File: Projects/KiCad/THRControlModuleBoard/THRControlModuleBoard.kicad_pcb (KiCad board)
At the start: 2 copper layers, 137.4 x 137.4 mm, 63 parts, among them IC1 LTC1480CN8#PBF, IC2 LTC1480CN8#PBF, J1 Conn_01x02_Socket, J2 Conn_01x02_Socket, J3 PCC-SMP-K-5, J4 Screw_Terminal_01x02, J5 Conn_01x04_Socket, J6 Conn_01x04_Socket, Q1 Q_PMOS_GDS, Q2 Q_PMOS_GDS, Q3 Q_PMOS_GDS, U1 LTC4416EMS#PBF, U2 MAX31856MUD+T, U3 Value: MCP2562-E-P, U4 MCP2515-I/P, U5 MAX31855, Y1 8MHz

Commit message: 外形を大方決めた
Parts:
- removed the C1 at (85.2, 101.2)
- removed the C7 at (102.0, 113.5)
- removed the D1 at (75.4, 118.3)
- removed D5: LED, LED_SMD:LED_0805_2012Metric_Pad1.15x1.40mm_HandSolder
- removed the J1 at (79.9, 96.7)
- removed the J2 at (82.7, 120.3)
- removed JP3, JP4, JP5, JP6: SolderJumper_2_Bridged, Jumper:SolderJumper-2_P1.3mm_Open_TrianglePad1.0x1.5mm
- removed Q1, Q2, Q3: Q_PMOS_GDS, Package_TO_SOT_SMD:ATPAK-2
- removed the R1 at (75.4, 122.2)
- removed the R2 at (73.3, 107.5)
- removed the R5 at (79.9, 107.5)
- removed the R6 at (76.6, 107.5)
- removed the U1 at (85.2, 112.4)
- added C13: 0.1u, Capacitor_SMD:C_0805_2012Metric_Pad1.18x1.45mm_HandSolder, F.Cu at (243.9, 32.5)
- added C14: 0.1u, Capacitor_SMD:C_0805_2012Metric_Pad1.18x1.45mm_HandSolder, F.Cu at (243.9, 35.5)
- added C15: 0.1u, Capacitor_SMD:C_0805_2012Metric_Pad1.18x1.45mm_HandSolder, F.Cu at (243.9, 38.5)
- added C16: 0.1u, Capacitor_SMD:C_0805_2012Metric_Pad1.18x1.45mm_HandSolder, F.Cu at (243.9, 41.5)
- added C17: 0.1u, Capacitor_SMD:C_0805_2012Metric_Pad1.18x1.45mm_HandSolder, F.Cu at (243.9, 44.5)
- added C18: 0.1u, Capacitor_SMD:C_0805_2012Metric_Pad1.18x1.45mm_HandSolder, F.Cu at (243.9, 47.5)
- added D4: D, Diode_SMD:D_SOD-123, F.Cu at (242.4, 58.5)
- added J3: Conn_02x03_Odd_Even, Connector_PinHeader_2.00mm:PinHeader_2x03_P2.00mm_Vertical, F.Cu at (89.0, 135.8)
- added J4: Conn_02x03_Odd_Even, Connector_PinHeader_2.00mm:PinHeader_2x03_P2.00mm_Vertical, F.Cu at (256.4, 33.0)
- added J7: Conn_02x03_Odd_Even, Connector_PinHeader_2.00mm:PinHeader_2x03_P2.00mm_Vertical, F.Cu at (104.3, 113.4)
- added LS1: PKB24SPCH3601-B0, PKB24SPCH3601-B0:SPKR_PKB24SPCH3601-B0, F.Cu at (193.8, 129.3)
- added R11: 10k, Resistor_SMD:R_0603_1608Metric_Pad0.98x0.95mm_HandSolder, F.Cu at (217.8, 60.6)
- added R12: 1k, Resistor_SMD:R_0603_1608Metric_Pad0.98x0.95mm_HandSolder, F.Cu at (217.8, 63.1)
- added R13: 10k, Resistor_SMD:R_0603_1608Metric_Pad0.98x0.95mm_HandSolder, F.Cu at (217.8, 65.6)
- added R14: 10k, Resistor_SMD:R_0603_1608Metric_Pad0.98x0.95mm_HandSolder, F.Cu at (217.8, 68.1)
- added R15: 10k, Resistor_SMD:R_0603_1608Metric_Pad0.98x0.95mm_HandSolder, F.Cu at (217.8, 70.6)
- added R16: 10k, Resistor_SMD:R_0603_1608Metric_Pad0.98x0.95mm_HandSolder, F.Cu at (222.2, 58.1)
- added R17: 10k, Resistor_SMD:R_0603_1608Metric_Pad0.98x0.95mm_HandSolder, F.Cu at (222.2, 60.6)
- added R18: 10k, Resistor_SMD:R_0603_1608Metric_Pad0.98x0.95mm_HandSolder, F.Cu at (222.2, 63.1)
- added R19: 10k, Resistor_SMD:R_0603_1608Metric_Pad0.98x0.95mm_HandSolder, F.Cu at (222.2, 65.6)
- added R20: 10k, Resistor_SMD:R_0603_1608Metric_Pad0.98x0.95mm_HandSolder, F.Cu at (222.2, 68.1)
- added R21: 10k, Resistor_SMD:R_0603_1608Metric_Pad0.98x0.95mm_HandSolder, F.Cu at (222.2, 70.6)
- added R22: 1k, Resistor_SMD:R_0603_1608Metric_Pad0.98x0.95mm_HandSolder, F.Cu at (226.5, 58.1)
- added R23: 1k, Resistor_SMD:R_0603_1608Metric_Pad0.98x0.95mm_HandSolder, F.Cu at (226.5, 60.6)
- added R24: 1k, Resistor_SMD:R_0603_1608Metric_Pad0.98x0.95mm_HandSolder, F.Cu at (226.5, 63.1)
- added R25: 1k, Resistor_SMD:R_0603_1608Metric_Pad0.98x0.95mm_HandSolder, F.Cu at (226.5, 65.6)
- added R26: 1k, Resistor_SMD:R_0603_1608Metric_Pad0.98x0.95mm_HandSolder, F.Cu at (226.5, 68.1)
- added U4: TLP222A, Package_DIP:DIP-4_W7.62mm, F.Cu at (167.7, 117.9)
- C1: renamed from C2; footprint Capacitor_SMD:C_0805_2012Metric_Pad1.18x1.45mm_HandSolder -> Capacitor_SMD:C_0603_1608Metric_Pad1.08x0.95mm_HandSolder
- C10: renamed from C11; moved to B.Cu
- C11: renamed from C12; moved to B.Cu
- C12: renamed from C10; value 0.1μF -> 0.1μ; moved to B.Cu
- C2: renamed from C3; footprint Capacitor_SMD:C_0805_2012Metric_Pad1.18x1.45mm_HandSolder -> Capacitor_SMD:C_0603_1608Metric_Pad1.08x0.95mm_HandSolder
- C3: renamed from C4; footprint Capacitor_SMD:C_0805_2012Metric_Pad1.18x1.45mm_HandSolder -> Capacitor_SMD:C_0603_1608Metric_Pad1.08x0.95mm_HandSolder
- C4: renamed from C5; footprint Capacitor_SMD:C_0805_2012Metric_Pad1.18x1.45mm_HandSolder -> Capacitor_SMD:C_0603_1608Metric_Pad1.08x0.95mm_HandSolder
- C5: renamed from C6; footprint Capacitor_SMD:C_0805_2012Metric_Pad1.18x1.45mm_HandSolder -> Capacitor_SMD:C_0603_1608Metric_Pad1.08x0.95mm_HandSolder
- C6: renamed from C15; value 0.1μF -> 0.1u; footprint Capacitor_SMD:C_0805_2012Metric_Pad1.18x1.45mm_HandSolder -> Capacitor_SMD:C_0603_1608Metric_Pad1.08x0.95mm_HandSolder; moved to B.Cu
- C7: renamed from C8; value 0.1μF -> 0.1u; footprint Capacitor_SMD:C_0805_2012Metric_Pad1.18x1.45mm_HandSolder -> Capacitor_SMD:C_0603_1608Metric_Pad1.08x0.95mm_HandSolder
- C8: renamed from C9; value 0.1μF -> 0.1u; footprint Capacitor_SMD:C_0805_2012Metric_Pad1.18x1.45mm_HandSolder -> Capacitor_SMD:C_0603_1608Metric_Pad1.08x0.95mm_HandSolder
- C9: renamed from C14; value 0.1μF -> 0.1u; footprint Capacitor_SMD:C_0805_2012Metric_Pad1.18x1.45mm_HandSolder -> Capacitor_SMD:C_0603_1608Metric_Pad1.08x0.95mm_HandSolder; moved to B.Cu
- D1: renamed from D2; footprint Diode_SMD:D_0805_2012Metric_Pad1.15x1.40mm_HandSolder -> Diode_SMD:D_SOD-123
- D2: renamed from D3; footprint Diode_SMD:D_0805_2012Metric_Pad1.15x1.40mm_HandSolder -> Diode_SMD:D_SOD-123
- D3: renamed from D4; footprint Diode_SMD:D_0805_2012Metric_Pad1.15x1.40mm_HandSolder -> Diode_SMD:D_SOD-123
- J2: renamed from J4; footprint TerminalBlock:TerminalBlock_Altech_AK300-2_P5.00mm -> MAX31856MUD_T:RS_PRO_611-8157
- R10: value 1K -> 300; footprint LED_SMD:LED_0805_2012Metric_Pad1.15x1.40mm_HandSolder -> Resistor_SMD:R_0603_1608Metric_Pad0.98x0.95mm_HandSolder
- R6: renamed from R11; value 120Ω -> 120
- R7: renamed from R12; value 120Ω -> 120
- R8: renamed from R13; value 120Ω -> 120
- R9: renamed from R14; value 10kΩ -> 10k; moved to B.Cu
- U1: renamed from U2; footprint Package_SO:TSSOP-14_4.4x5mm_P0.65mm -> MAX31856MUD_T:SOP65P640X110-14N
- moved R10 149.5 mm to (217.8, 58.1)
- moved H4 121.4 mm to (226.9, 119.1)
- moved U5 103.3 mm to (78.2, 57.6), turned to 90 degrees
- moved JP1 83.9 mm to (234.3, 84.0), turned to 0 degrees
- moved H2 81.9 mm to (226.9, 98.0)
- moved JP2 79.3 mm to (234.3, 87.5), turned to 0 degrees
- moved H3 77.0 mm to (226.9, 108.5)
- moved J2 63.4 mm to (98.8, 34.4)
- moved G*** 55.1 mm to (88.3, 150.9)
- moved G*** 48.5 mm to (156.6, 178.4)
- moved C7 40.6 mm to (88.4, 96.7)
- moved IC1 40.6 mm to (89.7, 103.0)
- moved J6 40.6 mm to (77.2, 116.1)
- moved C8 40.6 mm to (88.3, 109.0)
- moved J5 40.6 mm to (77.2, 102.5)
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- renumbered J3 to J1, R3 to R1, R4 to R2, R7 to R3, R8 to R4, R9 to R5, U3 to U2, U4 to U3
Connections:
- net CAN_H renamed CAN__H
- net CAN_L renamed CAN__L
- A1 pad 10: unconnected-(A1-D7-Pad10) -> Umbilical__launchPin
- A1 pad 11: unconnected-(A1-D8-Pad11) -> Umbilical__waitingPin
- A1 pad 19: unconnected-(A1-A0-Pad19) -> B3M_Servo__Open
- A1 pad 20: unconnected-(A1-A1-Pad20) -> B3M_Servo__Close
- A1 pad 21: unconnected-(A1-A2-Pad21) -> RS405_Servo__Open
- A1 pad 22: unconnected-(A1-A3-Pad22) -> RS405_Servo__Close
- A1 pad 25: unconnected-(A1-A6-Pad25) -> IO__Busser
- A1 pad 30: +12V -> Net-(A1-VIN)
- A1 pad 6: MAX31855__~{CS}-~{CS} -> RS485__ENABLE_RS405
- A1 pad 8: RS485__ENABLE_RS405 -> MAX31855__~{CS}-~{CS}
- D1 pad 1: Net-(D2-K) -> SPI__MOSI
- D2 pad 1: Net-(D3-K) -> SPI__SCLK
- D3 pad 1: Net-(D4-K) -> MAX31856__~{CS}-~{CS}
- R10 pad 1: Net-(D5-A) -> IO__Busser
- U1 pad 11: Net-(JP6-A) -> SPI__MISO
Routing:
- net +3.3V: track 180.5 -> 74.6 mm, vias 5 -> 3
- net SPI__MISO: track 93.6 -> 8.61 mm, vias 4 -> 2
- net MAX31855__~{CS}-~{CS}: track 66.3 -> 0.00 mm, vias 1 -> 0
- net RS485__RO-RX: track 47.9 -> 0.00 mm, vias 1 -> 0
- net +12V: track 38.7 -> 0.00 mm
- net RS485__ENABLE_RS405: track 37.0 -> 0.00 mm, vias 3 -> 0
- net RS485__ENABLE_B3M: track 31.6 -> 0.00 mm
- net +5V: track 39.7 -> 10.1 mm, vias 1 -> 0
- net SPI__MOSI: track 32.4 -> 4.51 mm, vias 2 -> 0
- net External Power Supply: track 27.3 -> 0.00 mm, vias 2 -> 0
- net Net-(U1-E1): track 25.2 -> 0.00 mm
- net MAX31856__~{CS}-~{CS}: track 29.1 -> 4.11 mm, vias 2 -> 0
- net RS485__DI-TX: track 22.9 -> 0.22 mm
- net Net-(Q1-G): track 20.1 -> 0.00 mm, vias 2 -> 0
- net CAN__TXD-TXCAN: track 18.3 -> 0.00 mm
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- removed copper zone on F.Cu, net /QMOS/3-3
- removed copper zone on F.Cu, net External Power Supply
- removed copper zone on F.Cu, net Internal Power Supply
- removed copper zone on F.Cu, net Main Power Supply
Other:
- board size 137.4 x 137.4 mm -> 87.2 x 130 mm
- board text added: "~{CS}"
- board text removed: "Nano Every"

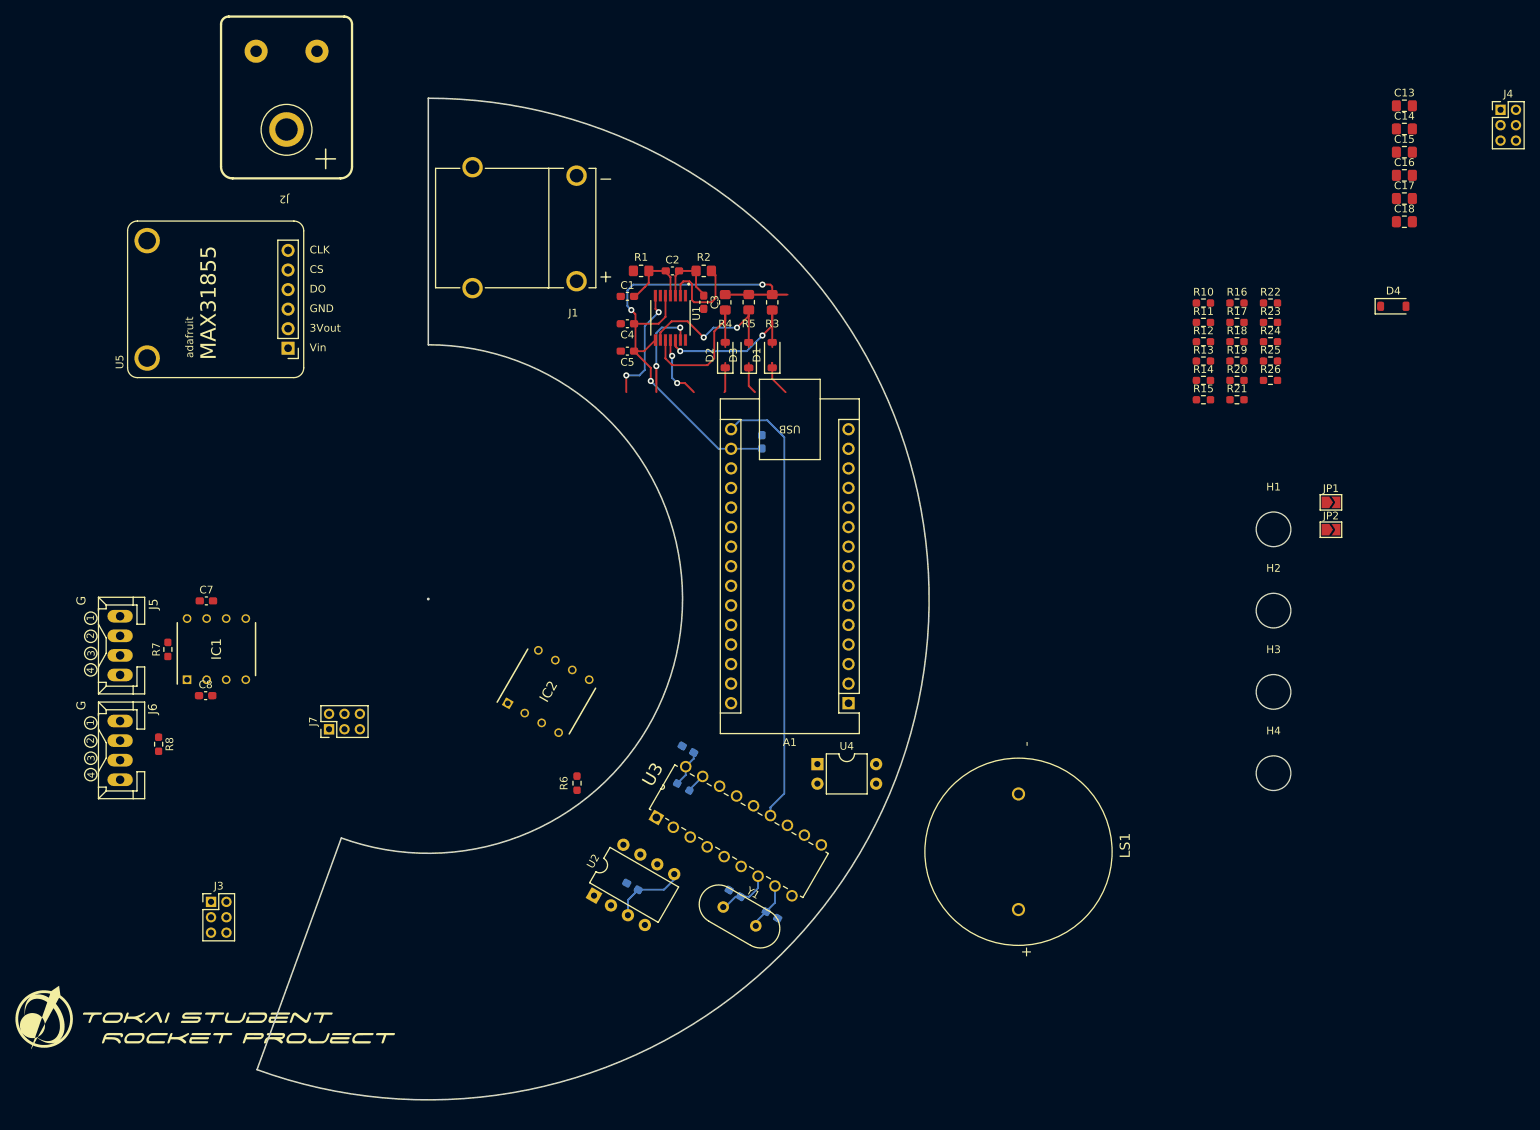
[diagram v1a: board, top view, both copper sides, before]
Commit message: 基板形状を決定。部品を配置中
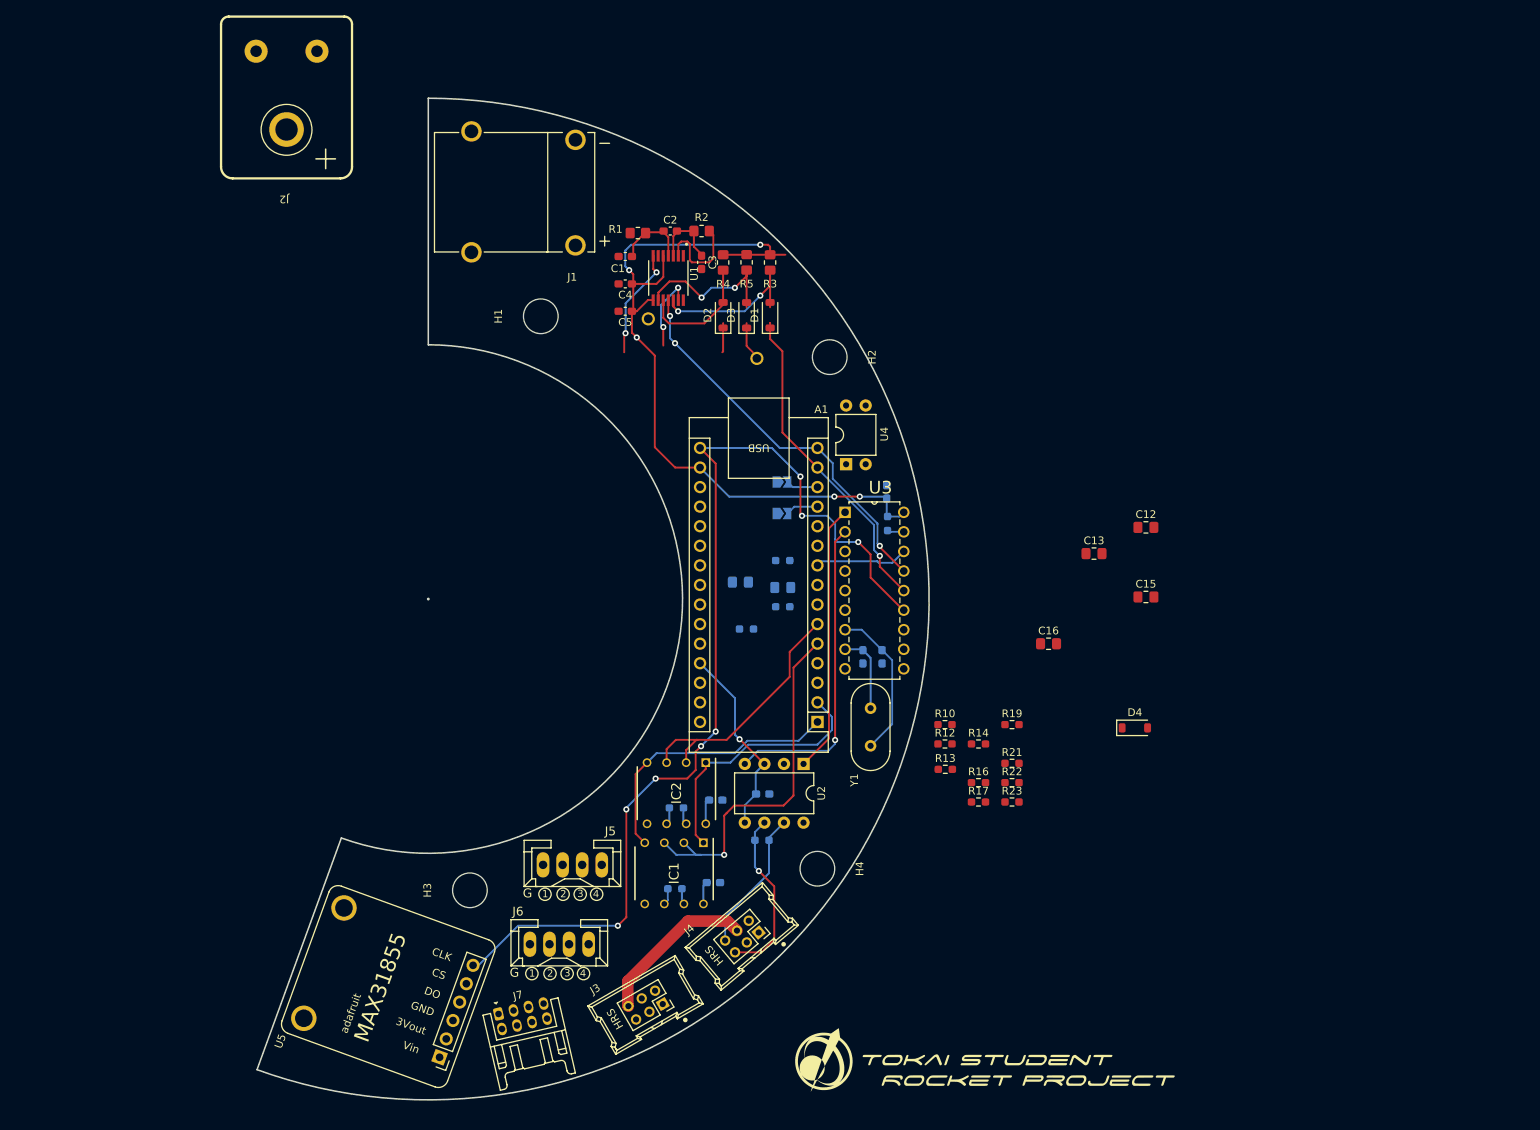
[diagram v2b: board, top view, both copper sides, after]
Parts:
- removed the C12 at (160.5, 76.1)
- removed the R13 at (217.8, 65.6)
- removed the R14 at (217.8, 68.1)
- removed the R15 at (217.8, 70.6)
- removed the R16 at (222.2, 58.1)
- C14: renamed from C15; moved to B.Cu
- C17: renamed from C18; moved to B.Cu
- C7, C8, JP1, JP2, LS1, R6, R7, R8: moved to B.Cu
- J3, J4: footprint Connector_PinHeader_2.00mm:PinHeader_2x03_P2.00mm_Vertical -> Hirose_Connector:Hirose_DF51A-6DP-2DSA
- J5, J6: value Conn_01x04_Socket -> Conn_01x04
- J7: value Conn_02x03_Odd_Even -> Conn_02x04_Odd_Even; footprint Connector_PinHeader_2.00mm:PinHeader_2x03_P2.00mm_Vertical -> Hirose_Connector:Hirose_DF11B-8DP-2DS
- R10: value 300 -> 620
- R15: renamed from R18; moved to B.Cu
- R18: renamed from R21; moved to B.Cu
- R20: renamed from R23; moved to B.Cu
- moved J4 145.6 mm to (157.9, 140.3), turned to 40 degrees
- moved H3 107.4 mm to (122.6, 134.3), turned to 90 degrees
- moved G*** 101.3 mm to (189.5, 156.4)
- moved H1 99.0 mm to (131.8, 59.8), turned to 90 degrees
- moved C14 98.5 mm to (163.2, 95.0), turned to 180 degrees
- moved C17 98.1 mm to (157.7, 94.3)
- moved U5 88.4 mm to (101.3, 142.9), turned to 70 degrees
- moved LS1 78.2 mm to (152.8, 62.7), turned to 160 degrees
- moved C7 75.3 mm to (154.2, 133.3)
- moved C16 74.0 mm to (197.7, 102.3)
- moved R7 72.8 mm to (149.2, 134.1), turned to 180 degrees
- moved JP2 71.5 mm to (163.1, 81.3)
- moved JP1 71.3 mm to (163.1, 85.4)
- moved R20 70.4 mm to (163.2, 91.5), turned to 180 degrees
- moved R18 70.3 mm to (158.5, 100.4), turned to 180 degrees
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- renumbered C13 to C12, C14 to C13, C16 to C15, C17 to C16, R11 to R12, R12 to R13, R17 to R14, R19 to R16, R20 to R17, R22 to R19, R24 to R21, R25 to R22, R26 to R23
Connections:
- net Net-(R10-Pad2) renamed /NanoEvery/PhotoMos_12Vin
- J3 pad 3: RS405_Servo__Openinput -> GND
- J3 pad 5: RS405_Servo__Closeinput -> GND
- J5 pad 1: RS485__B1 -> GND
- J5 pad 2: RS485__A1 -> +12V
- J5 pad 3: +12V -> RS485__A1
- J5 pad 4: GND -> RS485__B1
- J6 pad 1: RS485__B2 -> GND
- J6 pad 2: RS485__A2 -> +12V
- J6 pad 3: +12V -> RS485__A2
- J6 pad 4: GND -> RS485__B2
- J7 pad 2: +12V -> RS405_Servo__Openinput
- J7 pad 4: +15V -> RS405_Servo__Closeinput
- J7 pad 5: CAN_H -> GND
- J7 pad 6: CAN_L -> B3M_Servo__Openinput
- U5 pad 1: unconnected-(U5-+5V-Pad1) -> +3.3V
- U5 pad 2: +3.3V -> unconnected-(U5-Vout-Pad2)
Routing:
- net SPI__SCLK: track 62.0 -> 136.3 mm, vias 0 -> 8
- net RS485__ENABLE_B3M: track 0.00 -> 47.4 mm, vias 0 -> 1
- net SPI__MISO: track 8.61 -> 50.7 mm, vias 2 -> 3
- net CAN__RXD-CANRX: track 0.00 -> 40.9 mm, vias 0 -> 1
- net SPI__MOSI: track 4.51 -> 41.9 mm, vias 0 -> 1
- net RS485__DI-TX: track 0.22 -> 35.8 mm
- net CAN__TXD-TXCAN: track 0.00 -> 34.9 mm
- net +3.3V: track 74.6 -> 109.2 mm, vias 3 -> 5
- net RS485__RO-RX: track 0.00 -> 33.9 mm
- net RS485__ENABLE_RS405: track 0.00 -> 33.6 mm
- net CAN__L: track 0.00 -> 22.5 mm, vias 0 -> 1
- net +VDC: track 0.00 -> 21.2 mm
- net CAN__H: track 0.00 -> 18.5 mm
- net +5V: track 10.1 -> 25.2 mm, vias 0 -> 1
- net OCS2: track 7.08 -> 20.0 mm
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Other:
- board text removed: "~{CS}"

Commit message: 大方配線作業終わってきた。
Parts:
- C12, C13, C15, C16, R10, R12, R13, R14, R16, R17, R19, R21, R22, R23: moved to B.Cu
- moved C16 61.9 mm to (140.4, 125.8)
- moved D4 54.0 mm to (157.4, 129.6), turned to -90 degrees
- moved C15 53.2 mm to (158.8, 109.3), turned to 180 degrees
- moved R22 52.6 mm to (140.4, 122.6)
- moved C12 52.4 mm to (170.1, 120.8)
- moved R17 52.2 mm to (136.4, 125.8)
- moved R23 48.9 mm to (157.9, 88.8), turned to 180 degrees
- moved C13 42.1 mm to (163.6, 103.8)
- moved R10 40.6 mm to (172.8, 73.9)
- moved R21 36.2 mm to (158.8, 106.0), turned to 180 degrees
- moved R19 31.7 mm to (163.7, 100.5)
- moved R16 30.9 mm to (158.8, 112.5), turned to 180 degrees
- moved R14 26.1 mm to (163.8, 107.0)
- moved R12 16.6 mm to (170.2, 124.0)
- moved R13 14.2 mm to (170.2, 117.5)
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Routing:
- net RS405_Servo__Closeinput: track 0.00 -> 77.7 mm, vias 0 -> 3
- net RS405_Servo__Openinput: track 0.00 -> 66.7 mm, vias 0 -> 3
- net Umbilical__waitingInput: track 0.00 -> 65.7 mm, vias 0 -> 6
- net B3M_Servo__Openinput: track 0.00 -> 62.0 mm, vias 0 -> 3
- net +12V: track 0.00 -> 50.2 mm, vias 0 -> 2
- net IO__Busser: track 0.00 -> 46.5 mm, vias 0 -> 3
- net RS405_Servo__Open: track 0.00 -> 40.5 mm, vias 0 -> 2
- net B3M_Servo__Close: track 0.00 -> 40.2 mm
- net B3M_Servo__Closeinput: track 0.00 -> 35.3 mm, vias 0 -> 1
- net B3M_Servo__Open: track 0.00 -> 30.8 mm, vias 0 -> 2
- net Net-(A1-VIN): track 0.00 -> 18.9 mm, vias 0 -> 3
- net Umbilical__launchPin: track 0.00 -> 12.1 mm
- net RS405_Servo__Close: track 0.00 -> 10.2 mm, vias 0 -> 1
- net Net-(C13-Pad1): track 0.00 -> 7.60 mm
- net Net-(C12-Pad1): track 0.00 -> 7.40 mm
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
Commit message: 基本的な配線作業終了
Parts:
- moved J6 9.97 mm to (135.3, 131.4)
- moved J5 9.72 mm to (134.2, 141.3)
- moved H4 1.75 mm to (165.9, 131.5), turned to 90 degrees
- moved R17 1.33 mm to (135.3, 126.5)
- moved D1 1.09 mm to (162.7, 59.7)
- moved C16 1.05 mm to (139.3, 125.8)
- moved D2 0.91 mm to (154.6, 59.7)
- moved J1 0.60 mm to (128.3, 44.3)
- moved R22 0.35 mm to (140.8, 122.6)
- moved H2 0.21 mm to (168.2, 65.2)
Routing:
- net MAX31855__~{CS}-~{CS}: track 0.00 -> 107.4 mm, vias 0 -> 2
- net SPI__MISO: track 50.7 -> 150.1 mm, vias 2 -> 8
- net Umbilical__launchInput: track 0.00 -> 64.4 mm, vias 0 -> 3
- net +3.3V: track 105.2 -> 147.7 mm
- net MAX31856__~{CS}-~{CS}: track 0.00 -> 39.7 mm
- net DRDY: track 14.4 -> 47.7 mm, vias 2 -> 3
- net ~{FAULT}: track 10.2 -> 36.1 mm, vias 2 -> 3
- net RS485__A2: track 2.22 -> 22.6 mm
- net RS485__B2: track 2.22 -> 18.9 mm
- net RS485__A1: track 2.16 -> 17.8 mm
- net RS485__B1: track 2.08 -> 17.2 mm
- net SPI__SCLK: track 137.3 -> 150.5 mm
- net B3M_Servo__Closeinput: track 35.3 -> 31.5 mm
- net B3M_Servo__Openinput: track 62.0 -> 65.1 mm
- net RS405_Servo__Open: track 40.5 -> 43.1 mm, vias 2 -> 1
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
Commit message: 攻めた設計になってるけど動いてくれ…
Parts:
- removed G*** (x2): LOGO, LOGO
- removed the J1 at (128.3, 44.3)
- added D5: MM3Zxx, Diode_SMD:D_SOD-323F, B.Cu at (118.8, 131.5)
- added D6: LED, LED_SMD:LED_0603_1608Metric_Pad1.05x0.95mm_HandSolder, F.Cu at (147.1, 134.4)
- added R11: 300, Resistor_SMD:R_0603_1608Metric_Pad0.98x0.95mm_HandSolder, F.Cu at (157.3, 77.8)
- added R24: 1k, Resistor_SMD:R_0603_1608Metric_Pad0.98x0.95mm_HandSolder, B.Cu at (144.9, 135.9)
- D4: value D -> MM3Zxx; footprint Diode_SMD:D_SOD-123 -> Diode_SMD:D_SOD-323F
- U1: footprint MAX31856MUD_T:SOP65P640X110-14N -> Package_SO:TSSOP-14_4.4x5mm_P0.65mm
- moved D4 37.8 mm to (119.9, 134.2), turned to 180 degrees
- moved H4 21.2 mm to (145.1, 128.1), turned to -90 degrees
- moved H2 20.3 mm to (148.2, 62.2), turned to -90 degrees
- moved LS1 19.7 mm to (133.4, 58.9)
- moved H1 17.3 mm to (115.0, 55.6)
- moved C11 17.2 mm to (160.0, 98.0)
- moved J3 17.0 mm to (140.9, 139.8)
- moved J2 16.8 mm to (128.8, 147.3), turned to 27 degrees
- moved C6 15.0 mm to (146.4, 116.8)
- moved R16 14.9 mm to (144.7, 107.7)
- moved C15 14.8 mm to (144.6, 105.0)
- moved C7 14.8 mm to (138.4, 130.3)
- moved C16 14.7 mm to (125.0, 122.7)
- moved D3 14.7 mm to (144.2, 56.0), turned to 180 degrees
- moved R21 14.7 mm to (144.6, 102.0)
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- renumbered J2 to J1, J3 to J2, J4 to J3, J5 to J4, J6 to J5, J7 to J6
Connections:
- A1 pad 30: Net-(A1-VIN) -> +12V
- D4 pad 1: Net-(A1-VIN) -> +12V
- D4 pad 2: +12V -> GND
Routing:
- net +12V: track 50.5 -> 200.4 mm, vias 2 -> 8
- net +3.3V: track 147.7 -> 245.1 mm, vias 4 -> 10
- net Net-(J1-Pin_2): track 0.00 -> 21.8 mm
- net BIAS: track 12.5 -> 33.0 mm, vias 0 -> 2
- net Net-(A1-VIN): track 19.2 -> 0.00 mm, vias 3 -> 0
- net CAN__L: track 23.0 -> 39.4 mm, vias 1 -> 2
- net CAN__H: track 18.5 -> 30.1 mm, vias 0 -> 1
- net SPI__MISO: track 150.1 -> 156.7 mm, vias 8 -> 10
- net GND: track 0.00 -> 5.73 mm, vias 0 -> 16
- net RS405_Servo__Openinput: track 68.3 -> 72.9 mm
- net Net-(D2-A): track 15.1 -> 19.0 mm
- net MAX31856__~{CS}-~{CS}: track 39.7 -> 43.5 mm
- net CAN__TXD-TXCAN: track 36.8 -> 40.2 mm, vias 0 -> 2
- net Net-(D6-A): track 0.00 -> 3.39 mm, vias 0 -> 1
- net CAN__RXD-CANRX: track 40.9 -> 44.1 mm, vias 1 -> 5
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- added copper zone on B.Cu, net GND
- added copper zone on F.Cu, net GND
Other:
- outline, holes or cut-outs redrawn

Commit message: ボード図を更新
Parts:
- added G***: LOGO, LOGO, F.Cu at (127.5, 65.8)
- added G***: LOGO, LOGO, B.Cu at (94.4, 142.6)
- added G***: LOGO, LOGO, B.Cu at (100.3, 143.5)
- C12, C13, C14, C15, C16, C17: value 0.1u -> 0.1uF; footprint Capacitor_SMD:C_0805_2012Metric_Pad1.18x1.45mm_HandSolder -> Capacitor_SMD:C_0603_1608Metric_Pad1.08x0.95mm_HandSolder
- C6, C7, C8, C9: value 0.1u -> 0.1uF
- R9: footprint Resistor_SMD:R_0603_1608Metric_Pad0.98x0.95mm_HandSolder -> Resistor_SMD:R_0805_2012Metric_Pad1.20x1.40mm_HandSolder
- U2: value Value: MCP2562-E-P -> Value: Value: Value: MCP2562-E-P
- Y1: footprint Crystal:Crystal_HC49-U_Vertical -> Crystal:Crystal_HC49-4H_Vertical
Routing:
- net CAN__TXD-TXCAN: track 40.2 -> 39.7 mm
- net GND: vias 16 -> 40
